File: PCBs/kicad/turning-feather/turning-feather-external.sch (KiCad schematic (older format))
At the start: 10 parts, among them J3 In to J2, J4 In to J1, J4 RJ45 to targets, J5 Case micro socket, J6 micro plug -> HUZZAH32 socket, SW2 SW_Push_DPDT, SW3 Start/Stop, SW4 Face/Away

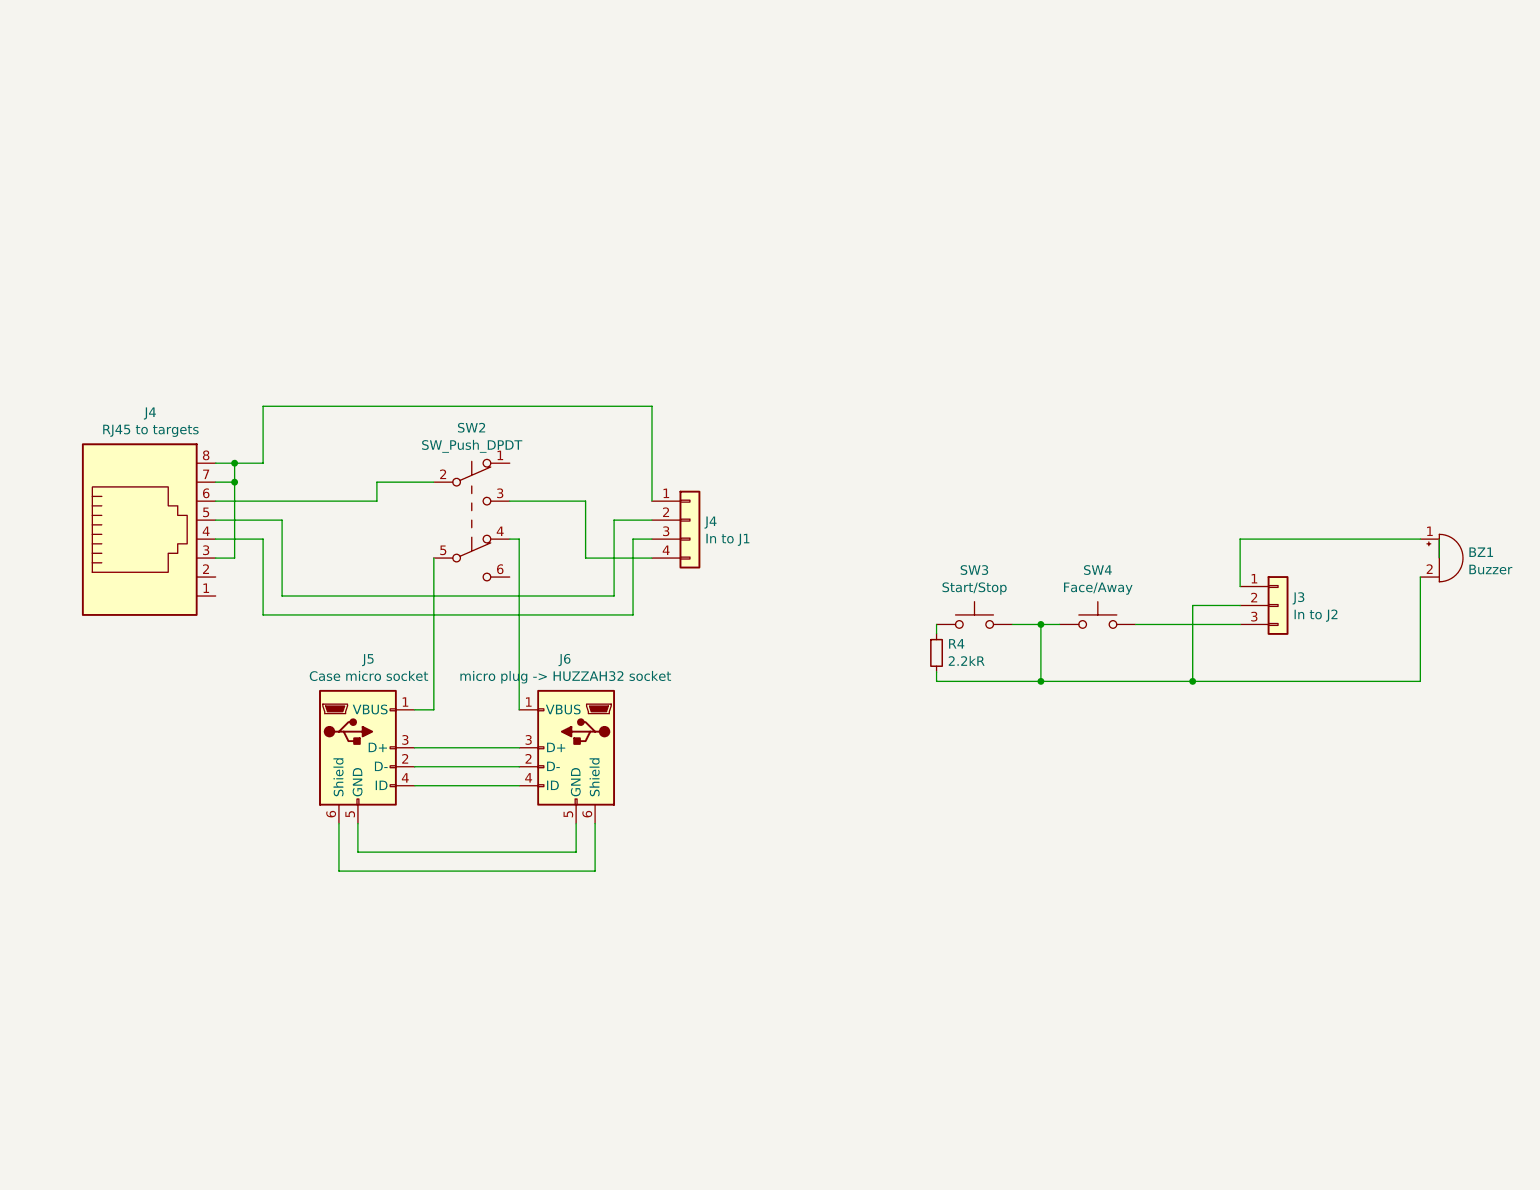
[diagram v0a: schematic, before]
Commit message: Update external schematic with options
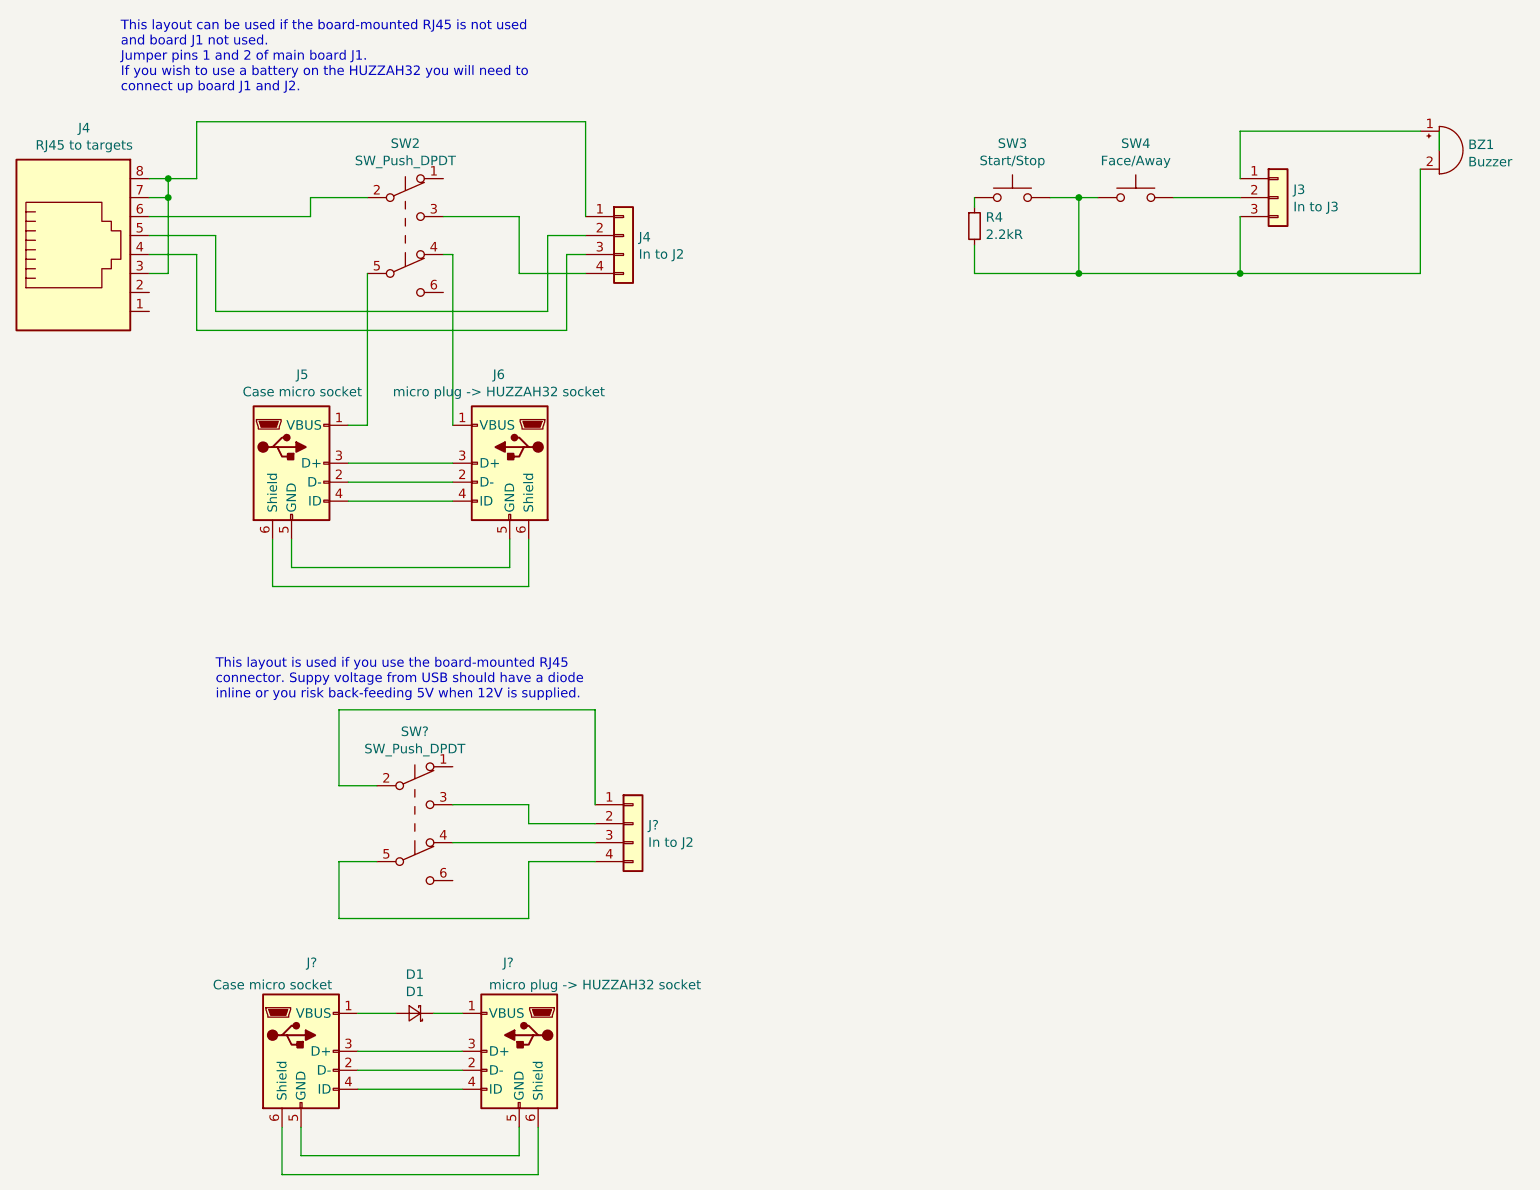
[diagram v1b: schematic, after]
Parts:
- added D1: D1, symbol Device:D_Schottky_Small
- added J?: micro plug -> HUZZAH32 socket, symbol Connector:USB_B_Micro
- added J?: Case micro socket, symbol Connector:USB_B_Micro
- added J?: In to J2, symbol Connector_Generic:Conn_01x04
- added SW?: SW_Push_DPDT, symbol Switch:SW_Push_DPDT
- J3: value In to J2 -> In to J3
- J4: value In to J1 -> In to J2
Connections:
- wire segments 53 -> 76
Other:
- note added: "This layout can be used if the board-mounted RJ45 is not used\nand board J1 not used.\nJumper pins 1 and 2 of main board J1.\nIf you wish to use a battery on the HUZZAH32 you will need to\nconnect up board J1 and J2."
- note added: "This layout is used if you use the board-mounted RJ45\nconnector. Suppy voltage from USB should have a diode\ninline or you risk back-feeding 5V when 12V is supplied."
- moved on the sheet: BZ1, J3, J4, J5, J6, R4, SW2, SW3, SW4

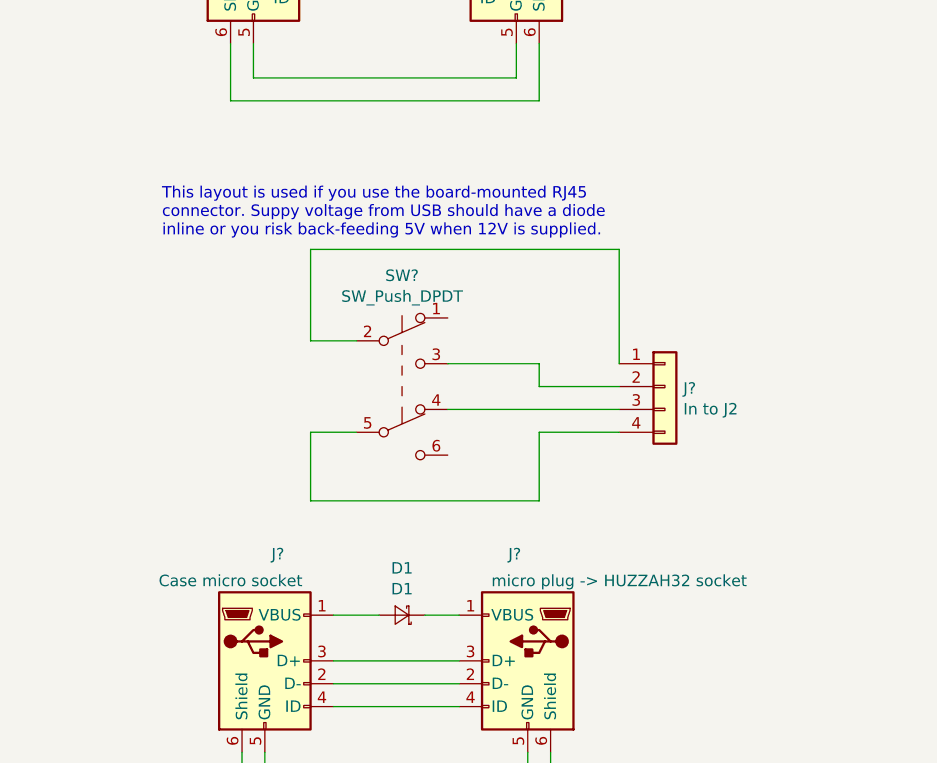
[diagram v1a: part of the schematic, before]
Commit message: Label diode and add text to external schema
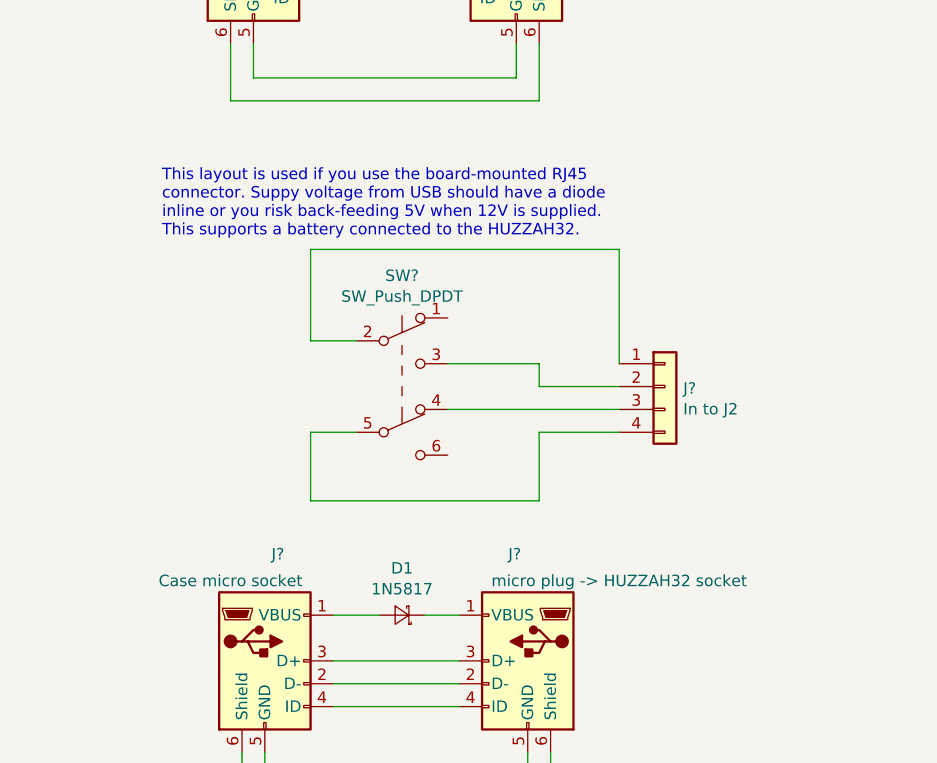
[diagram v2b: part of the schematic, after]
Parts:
- D1: value D1 -> 1N5817
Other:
- note added: "This layout is used if you use the board-mounted RJ45\nconnector. Suppy voltage from USB should have a diode\ninline or you risk back-feeding 5V when 12V is supplied.\nThis supports a battery connected to the HUZZAH32."
- note removed: "This layout is used if you use the board-mounted RJ45\nconnector. Suppy voltage from USB should have a diode\ninline or you risk back-feeding 5V when 12V is supplied."
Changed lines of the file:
@@
 P 4100 6050
 F 0 "D1" H 4100 5845 50  0000 C CNN
-F 1 "D1" H 4100 5936 50  0000 C CNN
+F 1 "1N5817" H 4100 5936 50  0000 C CNN
 F 2 "" V 4100 6050 50  0001 C CNN
 F 3 "~" V 4100 6050 50  0001 C CNN
@@
 	3700 5550 4700 5550
 Text Notes 3050 4400 0    50   ~ 0
-This layout is used if you use the board-mounted RJ45\nconnector. Suppy voltage from USB should have a diode\ninline or you risk back-feeding 5V when 12V is supplied.
+This layout is used if you use the board-mounted RJ45\nconnector. Suppy voltage from USB should have a diode\ninline or you risk back-feeding 5V when 12V is supplied.\nThis supports a battery connected to the HUZZAH32.
 $EndSCHEMATC
